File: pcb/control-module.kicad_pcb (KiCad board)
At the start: 2 copper layers, 78.7 x 69.9 mm, 110 parts, among them J1 Screw_Terminal_01x06, J2 Conn_01x07_Pin, J3 USB_C_Receptacle_USB2.0_16P, J4 Micro_SD_Card, J5 Conn_ST_STDC14, P1_CONT TestPoint, P1_FIRE TestPoint, P1_GNDD TestPoint, P1_OUT TestPoint, P2_CONT TestPoint, P2_FIRE TestPoint, P2_GNDD TestPoint, P2_OUT TestPoint, Q1 SiS454DN, Q2 SiS454DN, SW1 SW_DIP_x04, U1 TPS2116DRL, U2 USBLC6-2SC6, U3 STM32U545RETxQ, U4 MS5607-02BA, U5 LSM6DSL, U6 MCP73831-2-OT, U7 MIC5504-3.3YM5

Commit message: Push to Master Branch
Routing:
- net /IMU Sensors/imu_mosi: track 49.4 -> 47.7 mm
- net /MCU/PYRO2_FIRE: track 52.7 -> 51.3 mm
- net /IMU Sensors/imu_miso: track 51.8 -> 50.7 mm
- net /IMU Sensors/imu_int1: track 58.9 -> 58.2 mm

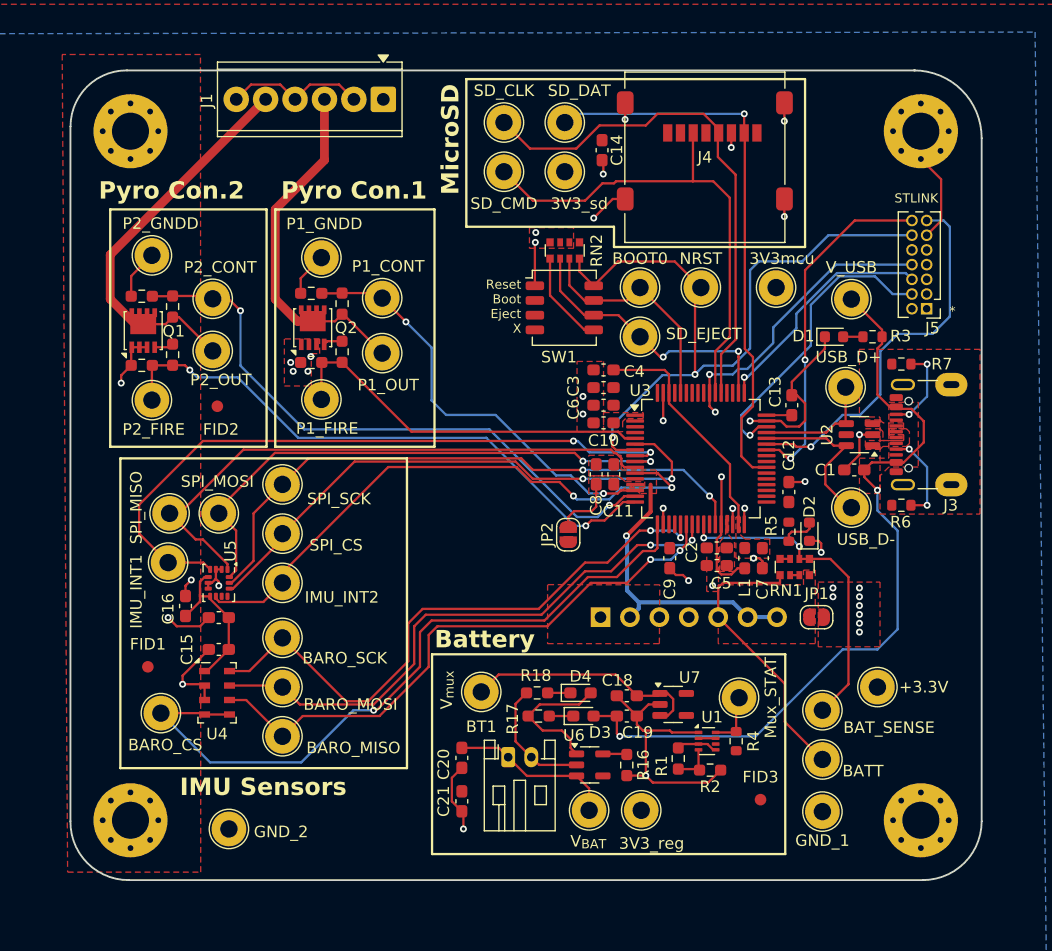
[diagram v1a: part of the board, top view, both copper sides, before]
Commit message: completed testbed board without GPS
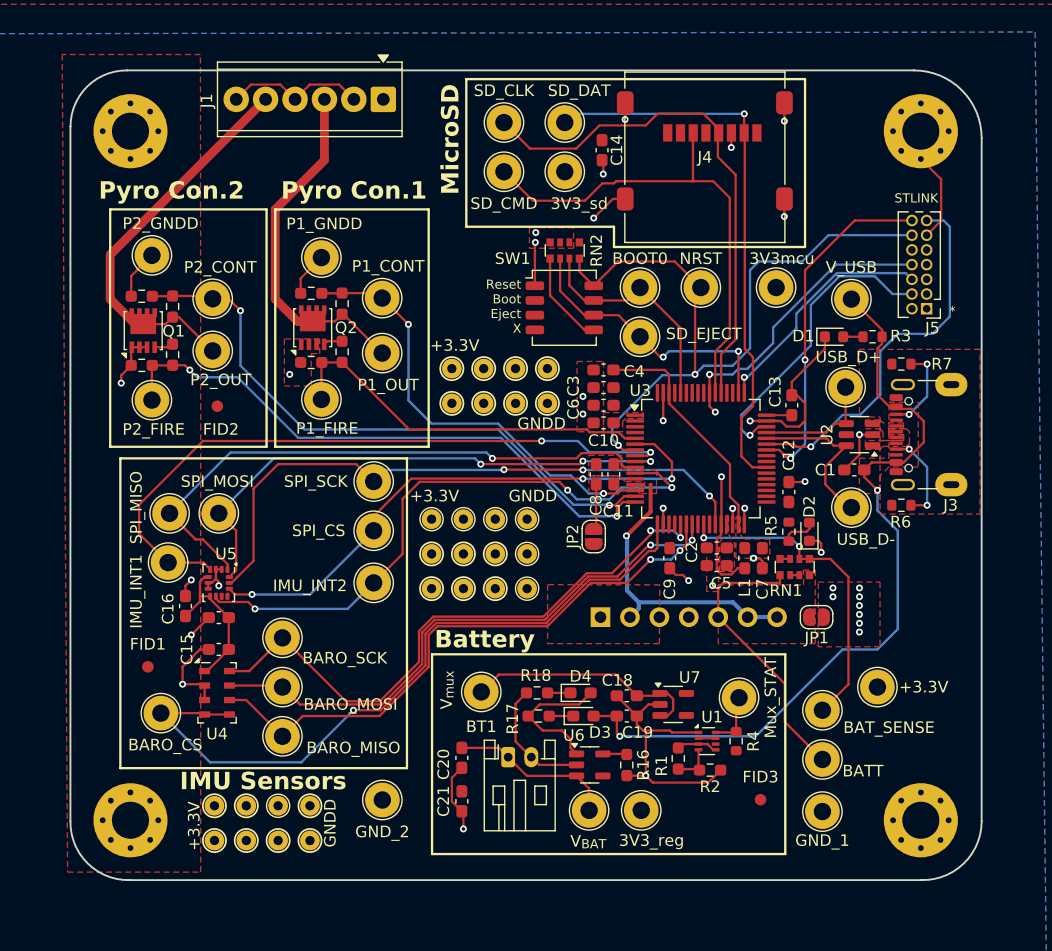
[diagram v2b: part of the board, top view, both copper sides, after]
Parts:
- added +3.3V: ProtoHole_0.8mm, TestPoint:TestPoint_THTPad_D2.0mm_Drill1.0mm, F.Cu at (146.5, 58.8)
- added ?: , , F.Cu at (146.5, 64.8)
- added ?: , , F.Cu at (153.8, 45.8)
- added ?: , , F.Cu at (151.0, 48.8)
- added ?: , , F.Cu at (156.5, 48.8)
- added ?: , , F.Cu at (156.5, 45.8)
- added ?: , , F.Cu at (136.0, 83.5)
- added ?: , , F.Cu at (146.5, 61.8)
- added ?: , , F.Cu at (136.0, 86.5)
- added ?: , , F.Cu at (127.8, 83.5)
- added ?: , , F.Cu at (127.8, 86.5)
- added ?: , , F.Cu at (133.2, 86.5)
- added ?: , , F.Cu at (151.0, 45.8)
- added ?: , , F.Cu at (148.2, 48.8)
- added ?: , , F.Cu at (130.5, 83.5)
- added ?: , , F.Cu at (153.8, 48.8)
- added ?: , , F.Cu at (152.0, 64.8)
- added ?: , , F.Cu at (130.5, 86.5)
- added ?: , , F.Cu at (149.2, 61.8)
- added ?: , , F.Cu at (152.0, 61.8)
- added ?: , , F.Cu at (148.2, 45.8)
- added ?: , , F.Cu at (149.2, 64.8)
- added GNDD: ProtoHole_0.8mm, TestPoint:TestPoint_THTPad_D2.0mm_Drill1.0mm, F.Cu at (152.0, 58.8)
- added GNDD: ProtoHole_0.8mm, TestPoint:TestPoint_THTPad_D2.0mm_Drill1.0mm, F.Cu at (149.2, 58.8)
- added GNDD: ProtoHole_0.8mm, TestPoint:TestPoint_THTPad_D2.0mm_Drill1.0mm, F.Cu at (154.8, 58.8)
- added GNDD: ProtoHole_0.8mm, TestPoint:TestPoint_THTPad_D2.0mm_Drill1.0mm, F.Cu at (133.2, 83.5)
- added REF**: ProtoHole_0.8mm, TestPoint:TestPoint_THTPad_D2.0mm_Drill1.0mm, F.Cu at (154.8, 61.8)
- added REF**: ProtoHole_0.8mm, TestPoint:TestPoint_THTPad_D2.0mm_Drill1.0mm, F.Cu at (154.8, 64.8)
- moved G*** 37.3 mm to (164.8, 50.1)
- moved GND_2 13.5 mm to (142.2, 83.0)
- moved SPI_CS 7.88 mm to (141.5, 59.8)
- moved SPI_SCK 7.88 mm to (141.5, 55.5)
- moved IMU_INT2 7.88 mm to (141.5, 64.2)
- moved JP2 2.21 mm to (160.5, 60.2)
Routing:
- net /IMU Sensors/imu_int2: track 50.3 -> 52.0 mm, vias 2 -> 3
- net /IMU Sensors/imu_sclk: track 52.3 -> 54.0 mm, vias 2 -> 3
- net VDDA: track 5.59 -> 3.94 mm
- net GNDD: track 125.9 -> 124.4 mm, vias 40 -> 37
- net /MCU/ADC1_IN5: track 37.0 -> 38.2 mm
- net /IMU Sensors/imu_miso: track 50.7 -> 51.7 mm, vias 0 -> 1
- net /IMU Sensors/imu_cs: track 48.9 -> 49.8 mm, vias 2 -> 3
- net /MCU/ADC1_IN6: track 53.1 -> 52.3 mm
- net /IMU Sensors/imu_mosi: track 47.7 -> 47.3 mm, vias 2 -> 3
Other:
- outline, holes or cut-outs redrawn
- board text added: "Control Module Testbed"
- board text added: "GNDD"
- board text removed: "+12V"
- board text removed: "Control Module Rev. 1"
- board text removed: "Energize"

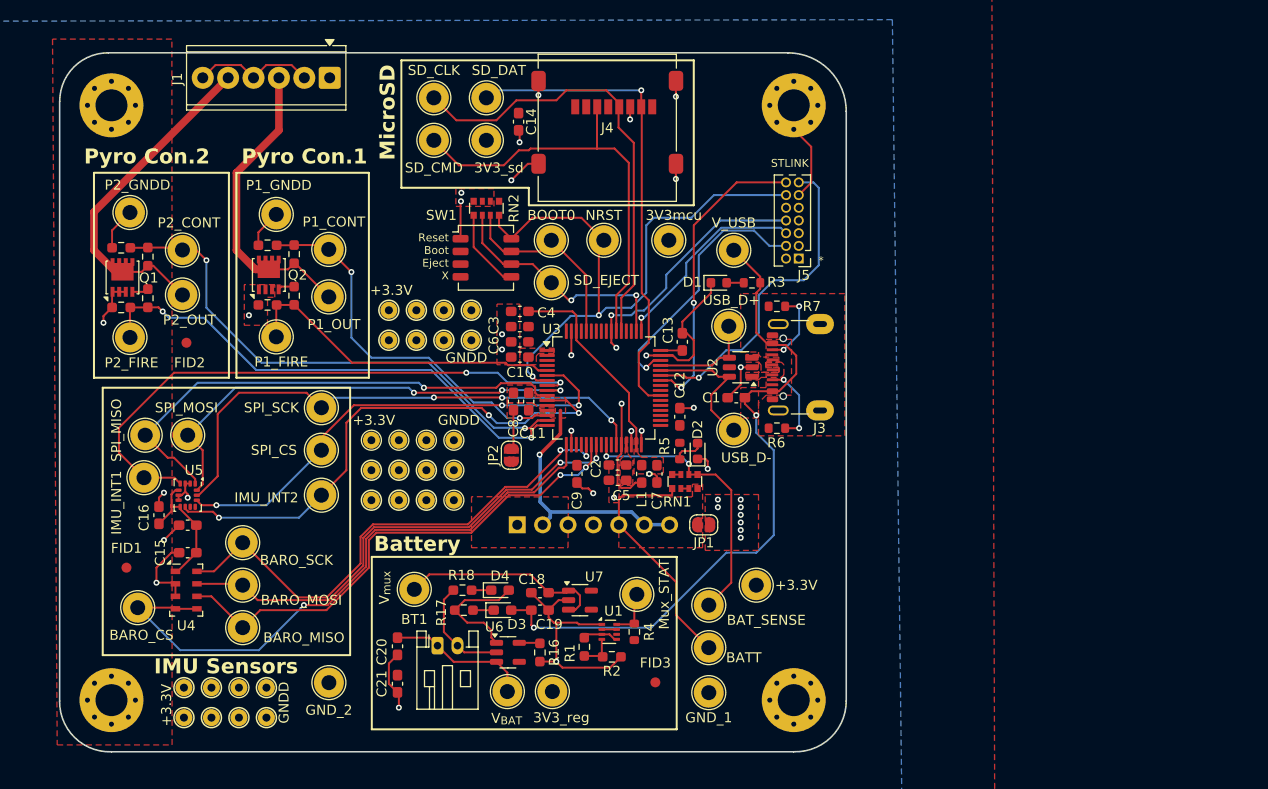
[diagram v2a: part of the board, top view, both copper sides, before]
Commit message: transmitter value update
updated some values for transmitter
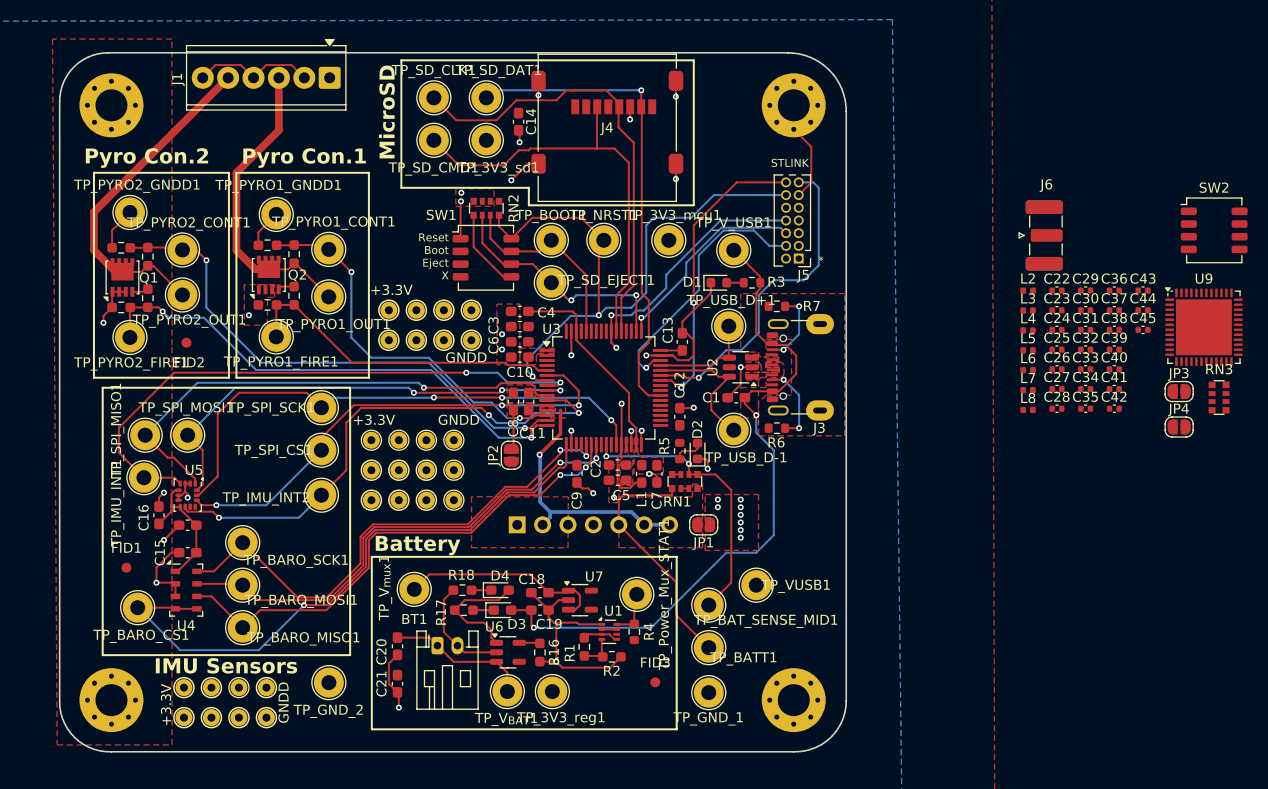
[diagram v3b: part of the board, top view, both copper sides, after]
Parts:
- added C22: C, Capacitor_SMD:C_0402_1005Metric, F.Cu at (215.1, 43.8)
- added C23: C, Capacitor_SMD:C_0402_1005Metric, F.Cu at (215.1, 45.8)
- added C24: C, Capacitor_SMD:C_0402_1005Metric, F.Cu at (215.1, 47.7)
- added C25: C, Capacitor_SMD:C_0402_1005Metric, F.Cu at (215.1, 49.7)
- added C26: C, Capacitor_SMD:C_0402_1005Metric, F.Cu at (215.1, 51.7)
- added C27: C, Capacitor_SMD:C_0402_1005Metric, F.Cu at (215.1, 53.6)
- added C28: C, Capacitor_SMD:C_0402_1005Metric, F.Cu at (215.1, 55.6)
- added C29: C, Capacitor_SMD:C_0402_1005Metric, F.Cu at (217.9, 43.8)
- added C30: C, Capacitor_SMD:C_0402_1005Metric, F.Cu at (217.9, 45.8)
- added C31: C, Capacitor_SMD:C_0402_1005Metric, F.Cu at (217.9, 47.7)
- added C32: C, Capacitor_SMD:C_0402_1005Metric, F.Cu at (217.9, 49.7)
- added C33: C, Capacitor_SMD:C_0402_1005Metric, F.Cu at (217.9, 51.7)
- added C34: C, Capacitor_SMD:C_0402_1005Metric, F.Cu at (217.9, 53.6)
- added C35: C, Capacitor_SMD:C_0402_1005Metric, F.Cu at (217.9, 55.6)
- added C36: C, Capacitor_SMD:C_0402_1005Metric, F.Cu at (220.8, 43.8)
- added C37: C, Capacitor_SMD:C_0402_1005Metric, F.Cu at (220.8, 45.8)
- added C38: C, Capacitor_SMD:C_0402_1005Metric, F.Cu at (220.8, 47.7)
- added C39: C, Capacitor_SMD:C_0402_1005Metric, F.Cu at (220.8, 49.7)
- added C40: C, Capacitor_SMD:C_0402_1005Metric, F.Cu at (220.8, 51.7)
- added C41: C, Capacitor_SMD:C_0402_1005Metric, F.Cu at (220.8, 53.6)
- added C42: C, Capacitor_SMD:C_0402_1005Metric, F.Cu at (220.8, 55.6)
- added C43: C, Capacitor_SMD:C_0402_1005Metric, F.Cu at (223.7, 43.8)
- added C44: C, Capacitor_SMD:C_0402_1005Metric, F.Cu at (223.7, 45.8)
- added C45: C, Capacitor_SMD:C_0402_1005Metric, F.Cu at (223.7, 47.7)
- added J6: Conn_Coaxial, Connector_Coaxial:SMA_Samtec_SMA-J-P-H-ST-EM1_EdgeMount, F.Cu at (214.1, 38.3)
- added JP3: SolderJumper_2_Open, Jumper:SolderJumper-2_P1.3mm_Open_RoundedPad1.0x1.5mm, F.Cu at (227.3, 53.9)
- added JP4: SolderJumper_2_Open, Jumper:SolderJumper-2_P1.3mm_Open_RoundedPad1.0x1.5mm, F.Cu at (227.3, 57.4)
- added L2: L, Inductor_SMD:L_0402_1005Metric, F.Cu at (212.2, 43.8)
- added L3: L, Inductor_SMD:L_0402_1005Metric, F.Cu at (212.2, 45.8)
- added L4: L, Inductor_SMD:L_0402_1005Metric, F.Cu at (212.2, 47.8)
- added L5: L, Inductor_SMD:L_0402_1005Metric, F.Cu at (212.2, 49.8)
- added L6: L, Inductor_SMD:L_0402_1005Metric, F.Cu at (212.2, 51.8)
- added L7: L, Inductor_SMD:L_0402_1005Metric, F.Cu at (212.2, 53.7)
- added L8: L, Inductor_SMD:L_0402_1005Metric, F.Cu at (212.2, 55.7)
- added RN3: 10k, Resistor_SMD:R_Array_Convex_4x0612, F.Cu at (231.3, 54.5)
- added SW2: SW_DIP_x04, Button_Switch_SMD:SW_DIP_SPSTx04_Slide_Copal_CHS-04A_W5.08mm_P1.27mm_JPin, F.Cu at (230.8, 37.8)
- added U9: STM32WL55CCUx, Package_DFN_QFN:QFN-48-1EP_7x7mm_P0.5mm_EP5.6x5.6mm, F.Cu at (229.8, 47.5)
- renumbered 3V3mcu to TP_3V3_mcu1, 3V3_reg to TP_3V3_reg1, 3V3_sd to TP_3V3_sd1, BARO_CS to TP_BARO_CS1, BARO_MISO to TP_BARO_MISO1, BARO_MOSI to TP_BARO_MOSI1, BARO_SCK to TP_BARO_SCK1, BATT to TP_BATT1, BAT_SENSE to TP_BAT_SENSE_MID1, BOOT0 to TP_BOOT1, GND_1 to TP_GND_1, GND_2 to TP_GND_2, IMU_INT1 to TP_IMU_INT1, IMU_INT2 to TP_IMU_INT2, NRST to TP_NRST1, P1_CONT to TP_PYRO1_CONT1, P1_FIRE to TP_PYRO1_FIRE1, P1_GNDD to TP_PYRO1_GNDD1, P1_OUT to TP_PYRO1_OUT1, P2_CONT to TP_PYRO2_CONT1, P2_FIRE to TP_PYRO2_FIRE1, P2_GNDD to TP_PYRO2_GNDD1, P2_OUT to TP_PYRO2_OUT1, Mux_STAT to TP_Power_Mux_STAT1, SD_CLK to TP_SD_CLK1, SD_CMD to TP_SD_CMD1, SD_DAT to TP_SD_DAT1, SD_EJECT to TP_SD_EJECT1, SPI_CS to TP_SPI_CS1, SPI_MISO to TP_SPI_MISO1, SPI_MOSI to TP_SPI_MOSI1, SPI_SCK to TP_SPI_SCK1, USB_D+ to TP_USB_D+1, USB_D- to TP_USB_D-1, +3.3V to TP_VUSB1, V_USB to TP_V_USB1, V_{BAT} to TP_V_{BAT}1, V_{mux} to TP_V_{mux}1

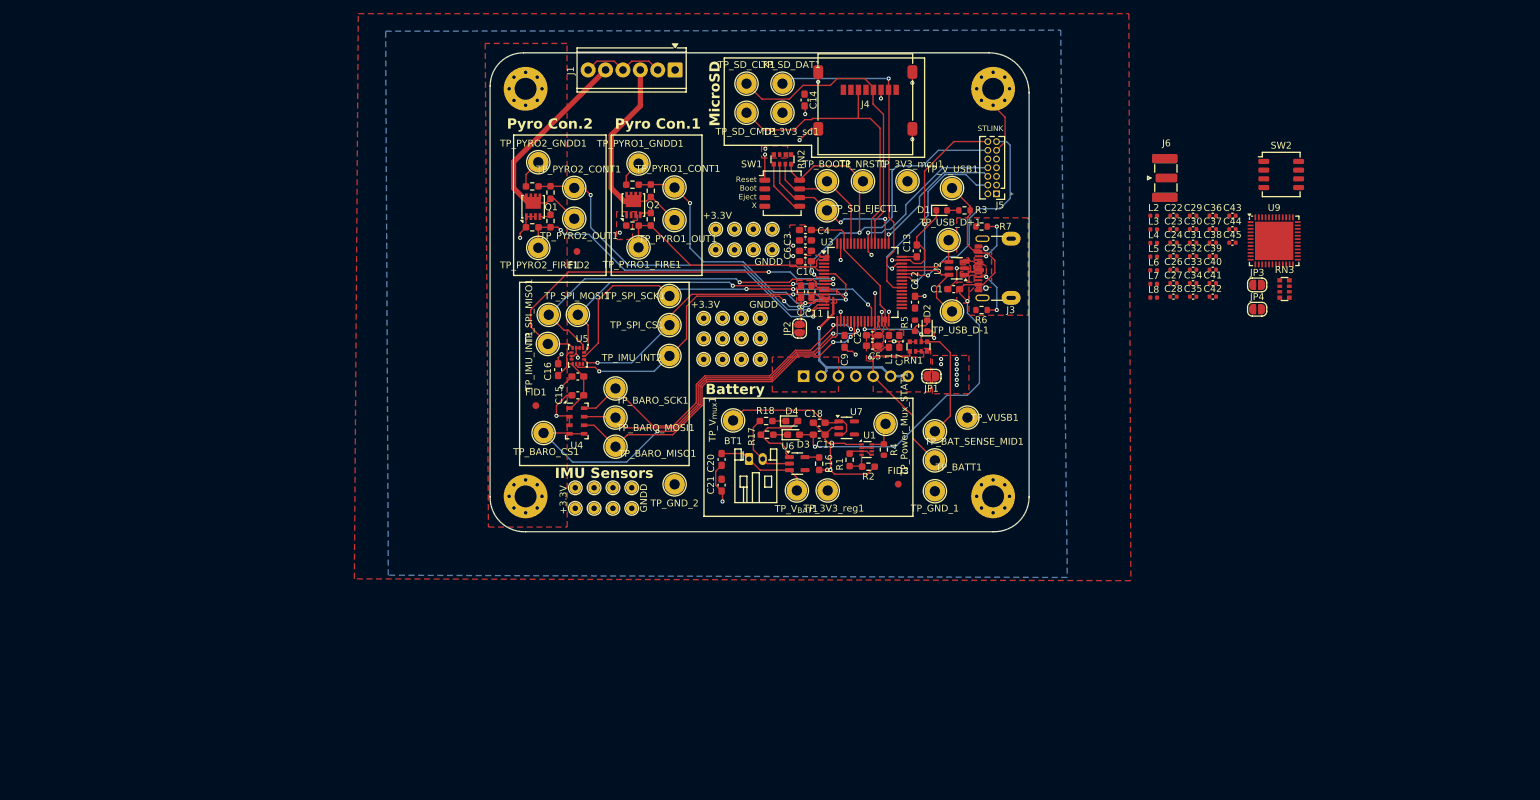
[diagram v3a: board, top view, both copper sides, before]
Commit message: Updated Board layout, finalized dimensions
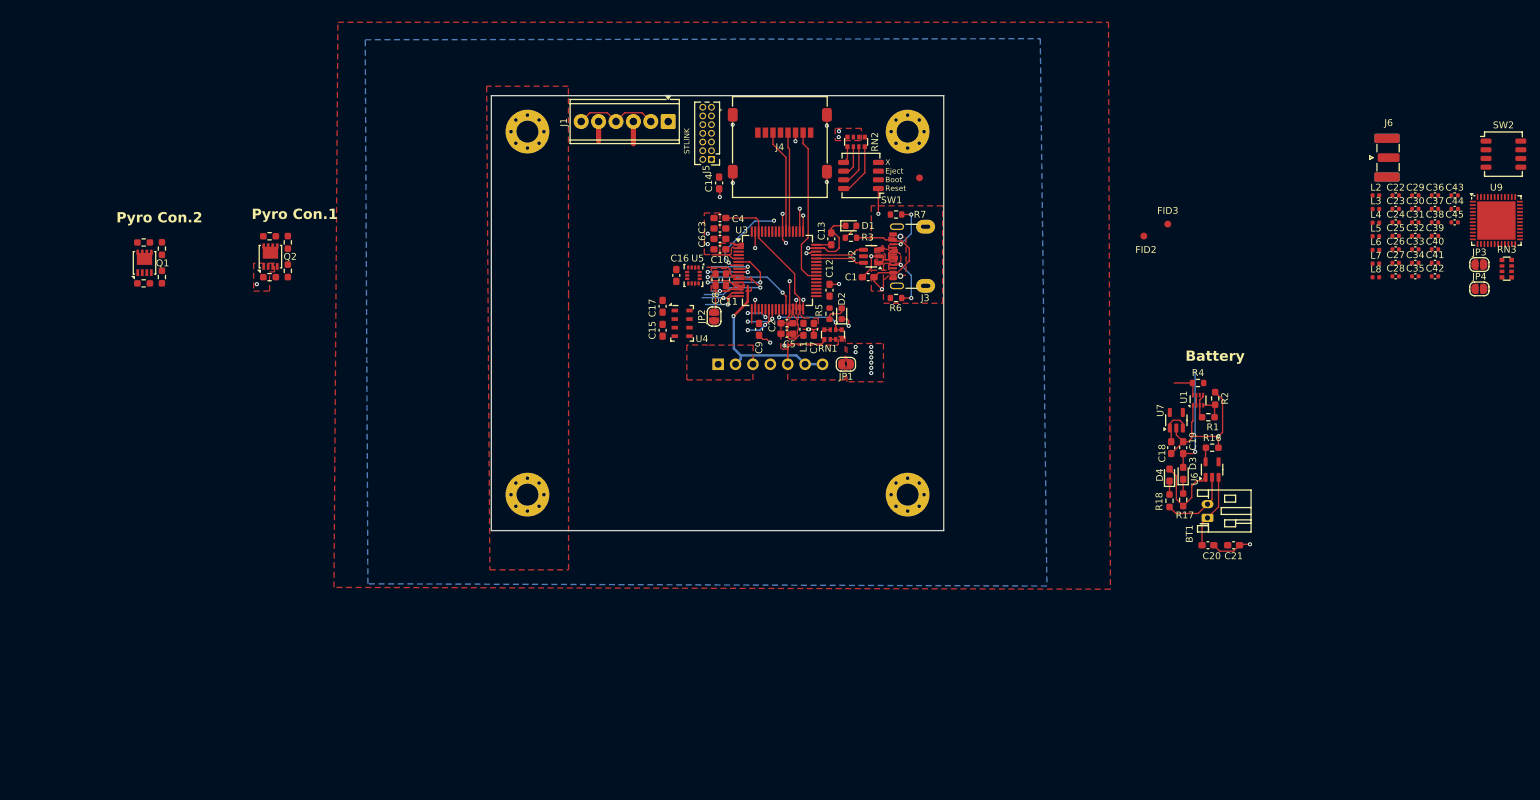
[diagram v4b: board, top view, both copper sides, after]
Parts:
- removed +3.3V, GNDD (x4), REF** (x2): ProtoHole_0.8mm, TestPoint:TestPoint_THTPad_D2.0mm_Drill1.0mm
- removed ? (x21): , 
- removed TP_3V3_mcu1, TP_3V3_reg1, TP_3V3_sd1, TP_BARO_CS1, TP_BARO_MISO1, TP_BARO_MOSI1, TP_BARO_SCK1, TP_BATT1, TP_BAT_SENSE_MID1, TP_BOOT1, TP_GND_1, TP_GND_2, TP_IMU_INT1, TP_IMU_INT2, TP_NRST1, TP_PYRO1_CONT1, TP_PYRO1_FIRE1, TP_PYRO1_GNDD1, TP_PYRO1_OUT1, TP_PYRO2_CONT1, TP_PYRO2_FIRE1, TP_PYRO2_GNDD1, TP_PYRO2_OUT1, TP_Power_Mux_STAT1, TP_SD_CLK1, TP_SD_CMD1, TP_SD_DAT1, TP_SD_EJECT1, TP_SPI_CS1, TP_SPI_MISO1, TP_SPI_MOSI1, TP_SPI_SCK1, TP_USB_D+1, TP_USB_D-1, TP_VUSB1, TP_V_USB1, TP_V_{BAT}1, TP_V_{mux}1: TestPoint, TestPoint:TestPoint_Loop_D2.54mm_Drill1.5mm_Beaded
- moved G*** 90.2 mm to (77.8, 26.5)
- moved FID2 82.8 mm to (210.8, 46.8)
- moved C21 75.3 mm to (223.9, 91.9), turned to 0 degrees
- moved C20 72.1 mm to (220.1, 91.9), turned to 0 degrees
- moved BT1 67.5 mm to (220.1, 87.9), turned to 90 degrees
- moved FID1 65.1 mm to (178.0, 38.2)
- moved R17 61.5 mm to (216.5, 85.2), turned to -90 degrees
- moved U6 60.6 mm to (220.7, 80.8), turned to 90 degrees
- moved R18 60.0 mm to (214.5, 85.4), turned to -90 degrees
- moved R16 57.4 mm to (220.7, 77.6), turned to 0 degrees
- moved R10 57.3 mm to (67.4, 48.6)
- moved R11 57.3 mm to (64.7, 47.7)
- moved R8 57.3 mm to (64.7, 53.7)
- moved R9 57.3 mm to (67.4, 52.7)
- moved Q1 57.3 mm to (64.9, 50.7)
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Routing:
- net /IMU Sensors/pres_cs: track 61.9 -> 2.05 mm, vias 1 -> 0
- net /IMU Sensors/imu_int1: track 58.2 -> 6.76 mm, vias 2 -> 1
- net /IMU Sensors/pres_sclk: track 51.9 -> 4.19 mm
- net /MCU/ADC1_IN6: track 52.3 -> 5.67 mm, vias 2 -> 1
- net /IMU Sensors/imu_miso: track 51.7 -> 5.43 mm, vias 1 -> 0
- net /IMU Sensors/pres_miso: track 51.1 -> 5.54 mm
- net /MCU/PYRO2_FIRE: track 51.0 -> 5.74 mm, vias 2 -> 1
- net /IMU Sensors/pres_mosi: track 49.4 -> 5.18 mm
- net /NRST: track 61.8 -> 20.4 mm
- net GNDD: track 124.4 -> 83.6 mm, vias 37 -> 33
- net /IMU Sensors/imu_mosi: track 47.3 -> 7.19 mm, vias 3 -> 2
- net /IMU Sensors/imu_int2: track 52.0 -> 12.3 mm, vias 3 -> 1
- net /IMU Sensors/imu_sclk: track 54.0 -> 14.5 mm, vias 3 -> 2
- net /IMU Sensors/imu_cs: track 49.8 -> 13.0 mm, vias 3 -> 2
- net +5V_USB: track 69.1 -> 34.1 mm
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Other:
- board size 78.7 x 69.9 mm -> 66 x 63.5 mm
- board text added: "C17"
- board text added: "X Eject Boot Reset"
- board text removed: "GNDD"
- board text removed: "IMU Sensors"
- board text removed: "MicroSD"
- board text removed: "Reset Boot Eject X"
